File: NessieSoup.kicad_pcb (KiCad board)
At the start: 2 copper layers, 84.7 x 50 mm, 3 parts, among them CN1 PLUS4_USERPORT, CN2 CONN_SNES_1, CN3 CONN_SNES_2

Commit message: Almost there
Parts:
- added V0: LICENSE, NessieSoup:cc_by_nc_sa_small, F.Cu at (134.9, 103.9)
- added V1: LOGO1, NessieSoup:Logo1, F.Cu at (147.1, 90.8)
- added V2: LOGO2, NessieSoup:Logo2, F.Cu at (157.2, 98.4)
- moved CN3 16.6 mm to (167.0, 69.7), turned to 120 degrees
- moved CN2 3.32 mm to (134.1, 70.0), turned to 240 degrees
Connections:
- net /data1 renamed /port1_d0
- net /data2 renamed /port2_d0
- CN1 pad 4: Net-(CN1-Pad4) -> /port2_d1
- CN1 pad 5: Net-(CN1-Pad5) -> /port2_pp
- CN3 pad 2: Net-(CN3-Pad2) -> /port2_pp
- CN3 pad 3: Net-(CN3-Pad3) -> /port2_d1
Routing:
- net /port2_pp: track 0.00 -> 43.9 mm, vias 0 -> 1
- net /port2_d1: track 0.00 -> 41.2 mm, vias 0 -> 1
- net +5V: track 92.5 -> 59.3 mm
- net /latch: track 81.7 -> 66.7 mm
- net /clock: track 83.3 -> 76.9 mm
- net /port1_d0: track 32.4 -> 37.3 mm
- net Net-(CN1-Pad7): track 3.25 -> 0.00 mm
- net Net-(CN1-Pad5): track 3.25 -> 0.00 mm
- net /port2_d0: track 38.9 -> 37.3 mm
- net GND: vias 0 -> 4
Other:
- board size 84.7 x 50 mm -> 65 x 63.2 mm
- board text added: "PORT 1"
- board text added: "PORT 2"
- board text added: "V1"
- board text added: "©2024 SukkoPera github.com/SukkoPera/NessieSoup"

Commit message: Add capacitor Yeah, we must have at least one component...
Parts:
- added C1: 47u, Capacitor_THT:CP_Radial_D5.0mm_P2.00mm, F.Cu at (168.0, 100.8)

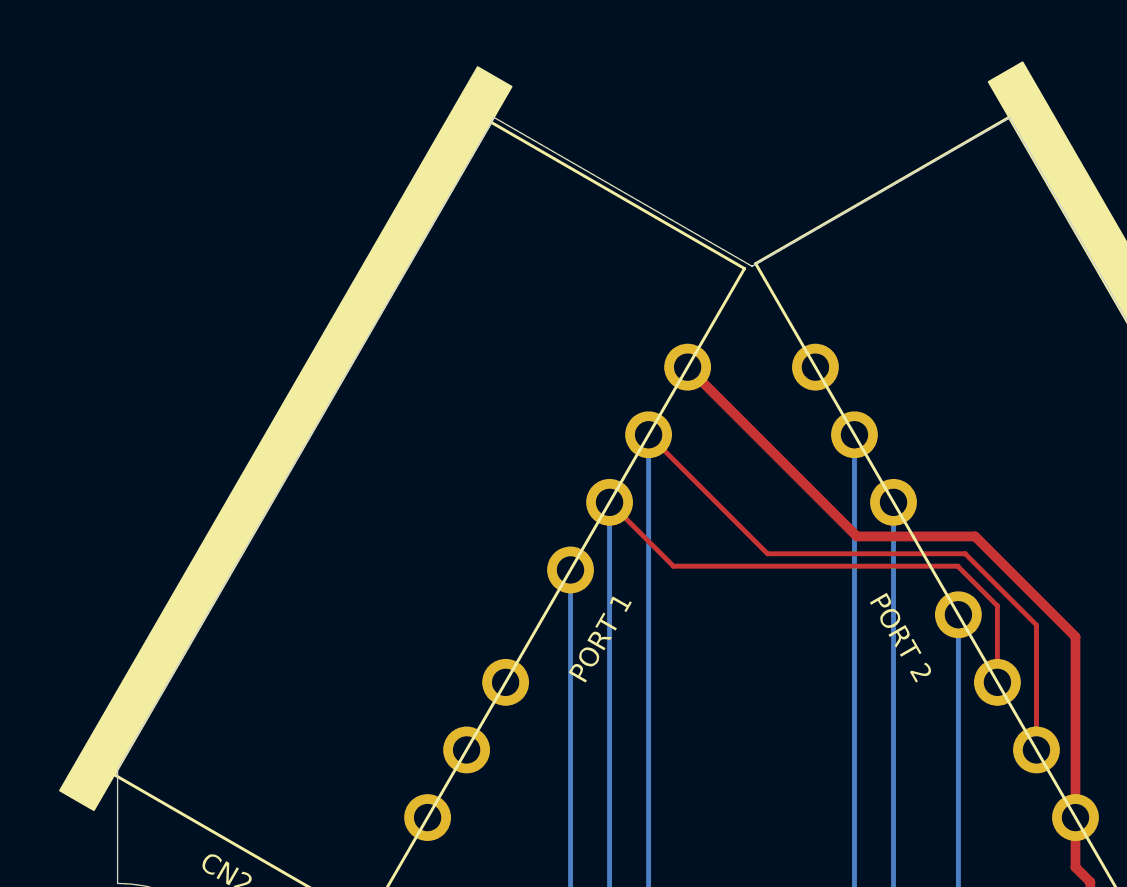
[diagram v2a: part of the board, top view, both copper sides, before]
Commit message: Refine shape
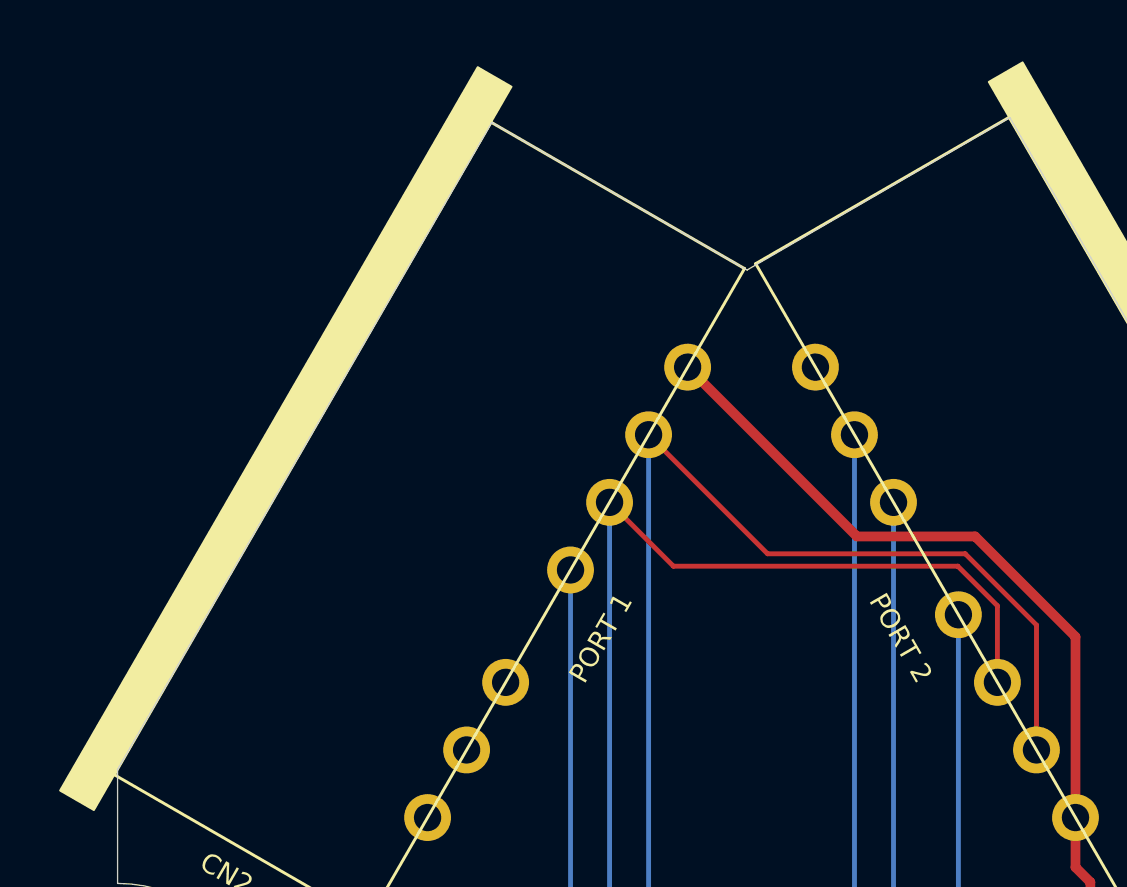
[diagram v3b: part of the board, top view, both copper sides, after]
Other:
- outline, holes or cut-outs redrawn

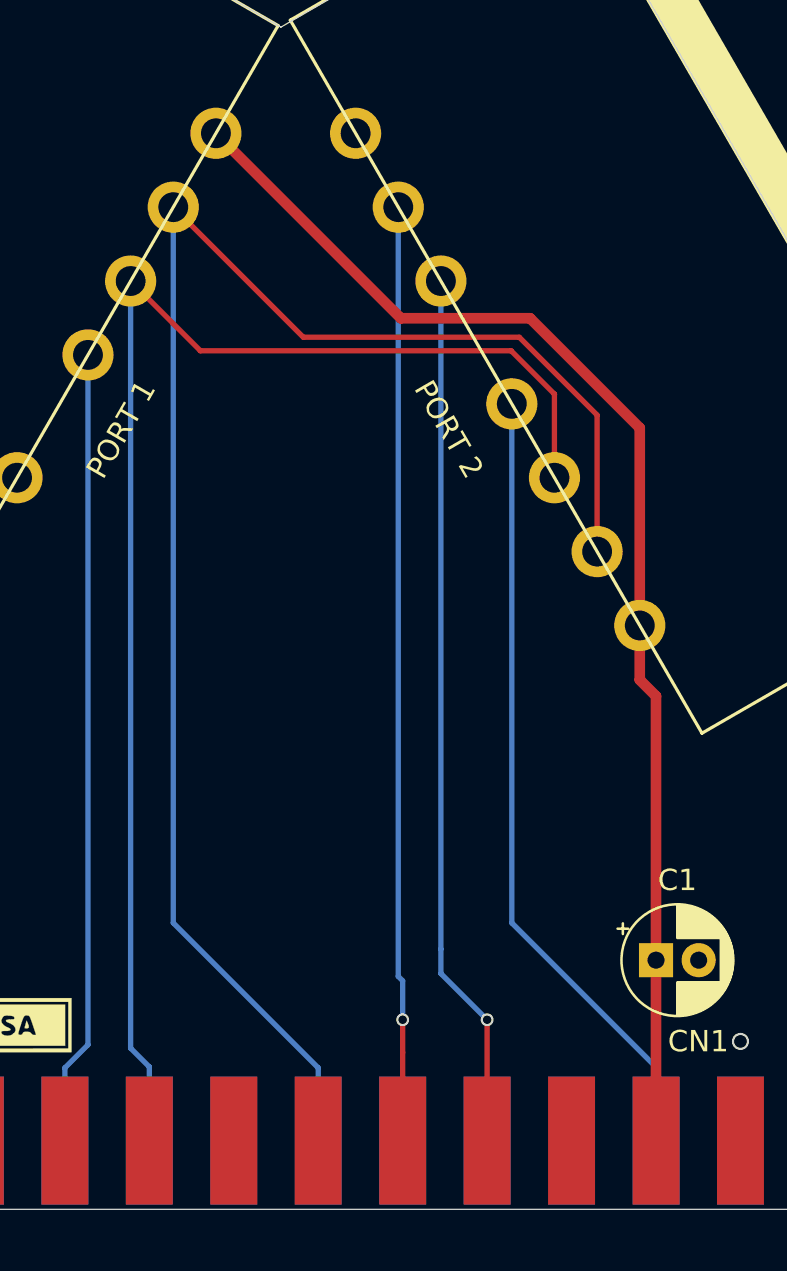
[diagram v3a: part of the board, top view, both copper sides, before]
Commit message: Add +4/C64 switch
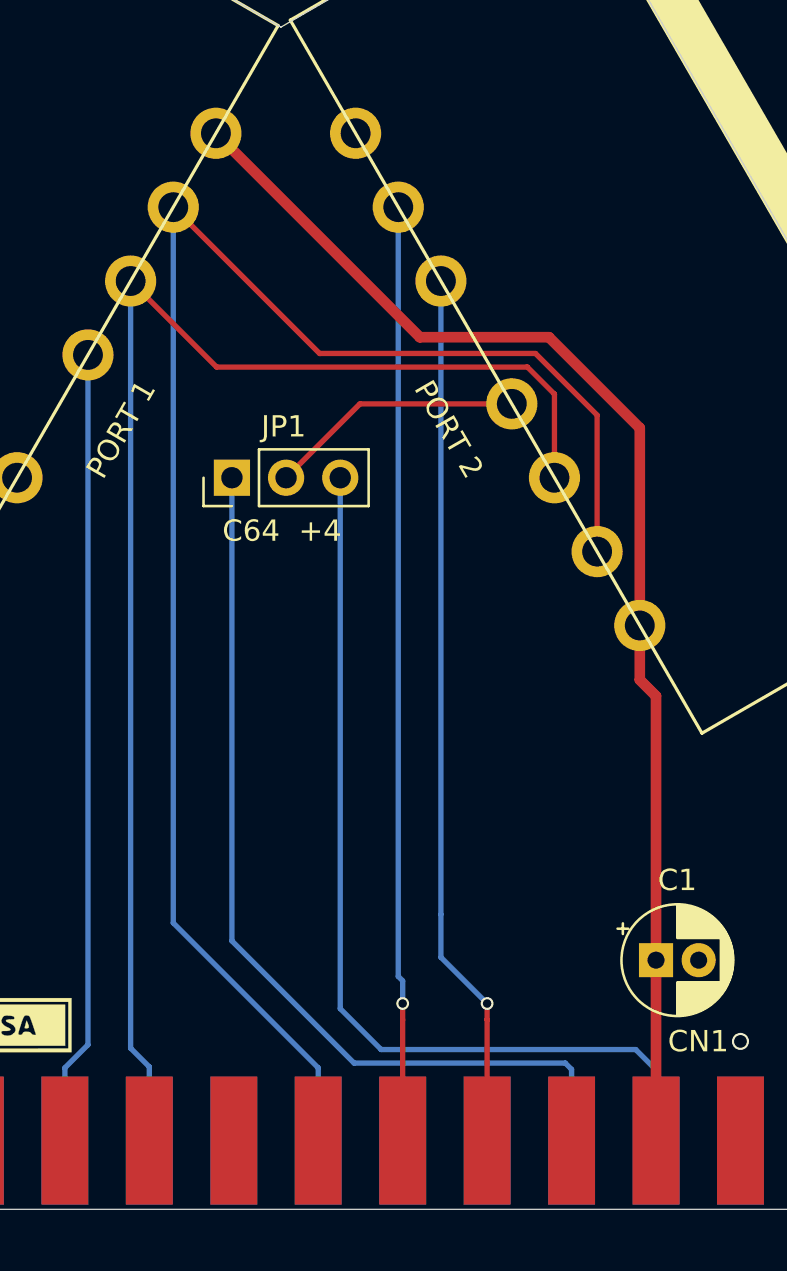
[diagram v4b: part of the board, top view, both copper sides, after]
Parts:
- added JP1: JMP_16_64, Connector_PinHeader_2.54mm:PinHeader_1x03_P2.54mm_Vertical, F.Cu at (148.1, 78.2)
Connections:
- CN1 pad B: /port2_d0 -> Net-(CN1-PadB)
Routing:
- net Net-(CN1-PadB): track 0.00 -> 44.2 mm
- net Net-(CN1-PadC): track 0.00 -> 43.5 mm
- net /port2_d0: track 37.3 -> 12.0 mm
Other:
- board text added: "+4"
- board text added: "C64"
